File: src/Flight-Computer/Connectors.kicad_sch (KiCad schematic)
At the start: 5 parts

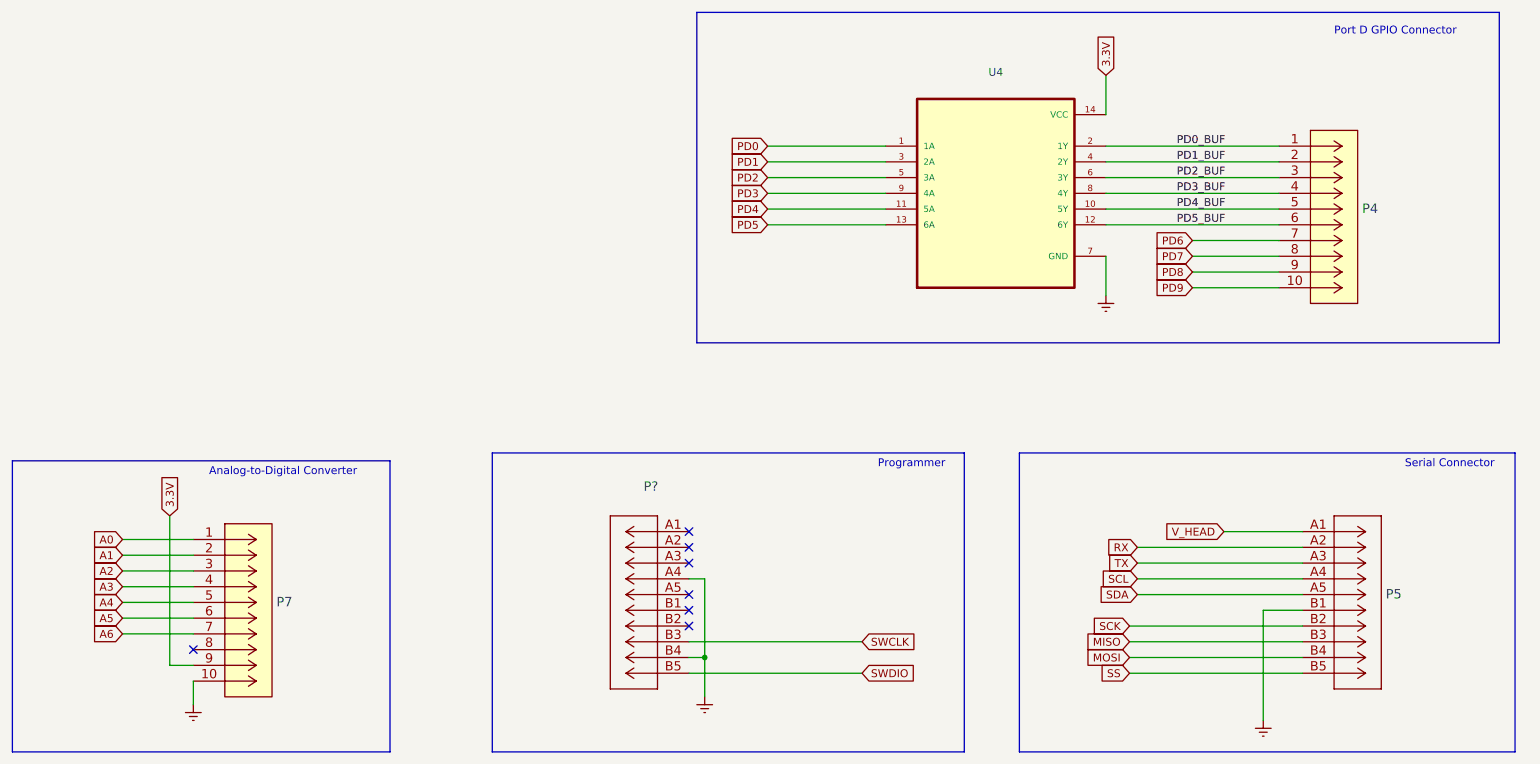
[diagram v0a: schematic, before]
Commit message: implemented crystal oscillator in schematic
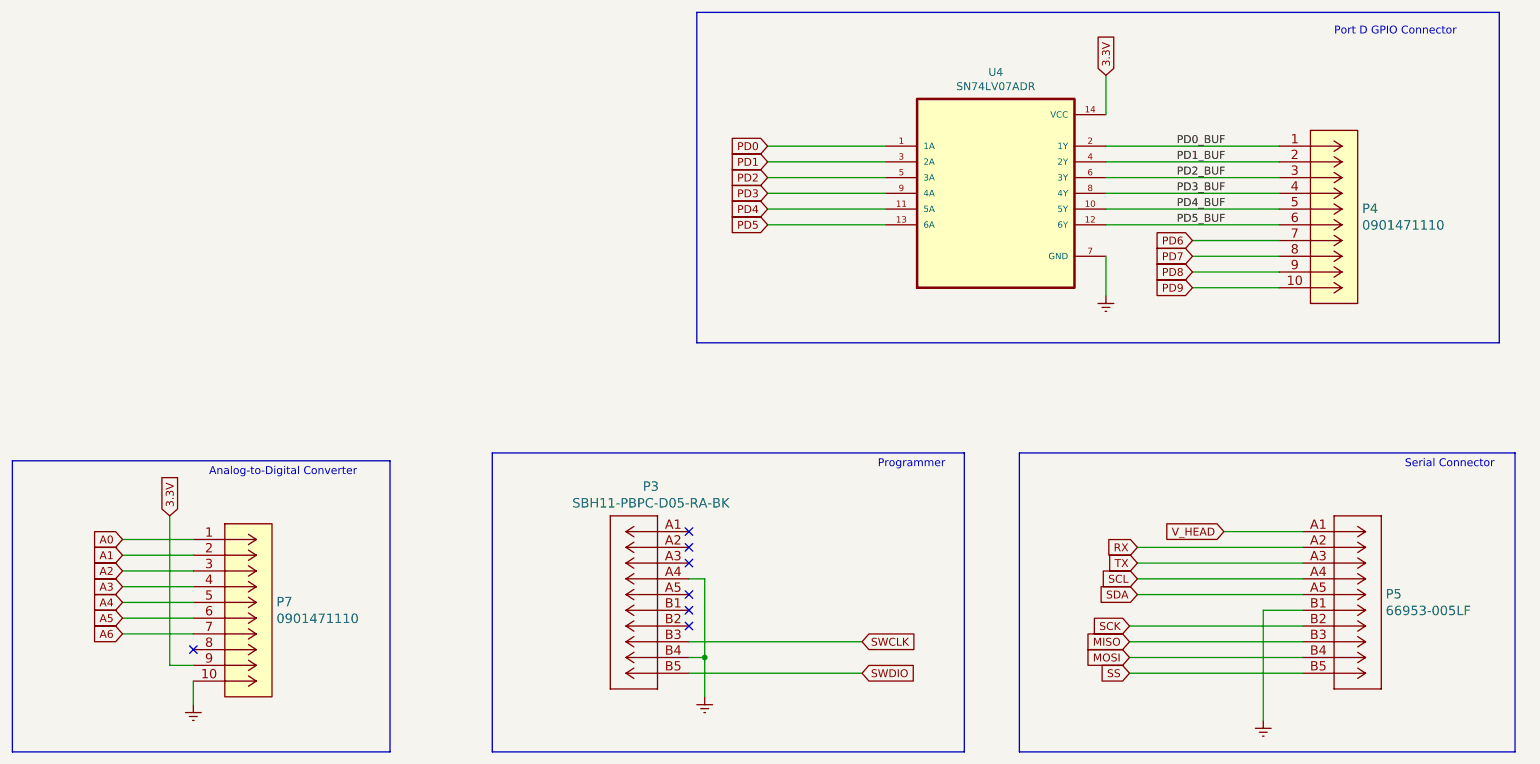
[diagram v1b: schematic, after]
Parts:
- P3: renamed from P?; value (none) -> SBH11-PBPC-D05-RA-BK; footprint (none) -> Engine-Controller:SBH11-PBPC-D05-RA-BK
- P4, P7: value (none) -> 0901471110; footprint (none) -> Engine-Controller:0901471110
- P5: value (none) -> 66953-005LF; footprint (none) -> Engine-Controller:66953-005LF
- U4: value (none) -> SN74LV07ADR; footprint (none) -> Engine-Controller:SN74LV07ADR
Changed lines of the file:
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@@
       (effects (font (size 1.27 1.27)) hide)
     )
-    (property "Value" "" (id 1) (at 223.52 146.05 0)
+    (property "Value" "Earth" (id 1) (at 223.52 146.05 0)
       (effects (font (size 1.27 1.27)) hide)
     )
@@
       (effects (font (size 1.524 1.524)) (justify left))
     )
-    (property "Value" "" (id 1) (at 239.4712 62.3062 0)
+    (property "Value" "0901471110" (id 1) (at 239.4712 62.3062 0)
       (effects (font (size 1.524 1.524)) (justify left))
     )
-    (property "Footprint" "" (id 2) (at 229.87 80.01 0)
+    (property "Footprint" "Engine-Controller:0901471110" (id 2) (at 229.87 80.01 0)
       (effects (font (size 1.524 1.524)) hide)
     )
@@
       (effects (font (size 1.524 1.524)) (justify left))
     )
-    (property "Value" "" (id 1) (at 243.2812 124.5362 0)
+    (property "Value" "66953-005LF" (id 1) (at 243.2812 124.5362 0)
       (effects (font (size 1.524 1.524)) (justify left))
     )
-    (property "Footprint" "" (id 2) (at 233.68 142.24 0)
+    (property "Footprint" "Engine-Controller:66953-005LF" (id 2) (at 233.68 142.24 0)
       (effects (font (size 1.524 1.524)) hide)
     )
@@
     (in_bom yes) (on_board yes)
     (property "Reference" "U4" (id 0) (at 180.34 37.592 0))
-    (property "Value" "" (id 1) (at 180.34 39.9034 0))
-    (property "Footprint" "" (id 2) (at 168.91 80.01 0)
+    (property "Value" "SN74LV07ADR" (id 1) (at 180.34 39.9034 0))
+    (property "Footprint" "Engine-Controller:SN74LV07ADR" (id 2) (at 168.91 80.01 0)
       (effects (font (size 1.27 1.27)) (justify left bottom) hide)
     )
@@
       (effects (font (size 1.27 1.27)) hide)
     )
-    (property "Value" "" (id 1) (at 198.12 77.47 0)
+    (property "Value" "Earth" (id 1) (at 198.12 77.47 0)
       (effects (font (size 1.27 1.27)) hide)
     )
@@
   (symbol (lib_id "Flight-Computer-rescue:Earth-power") (at 133.35 138.43 0) (unit 1)
     (in_bom yes) (on_board yes)
-    (property "Reference" "#PWR?" (id 0) (at 133.35 144.78 0)
+    (property "Reference" "#PWR06" (id 0) (at 133.35 144.78 0)
       (effects (font (size 1.27 1.27)) hide)
     )
-    (property "Value" "" (id 1) (at 133.35 142.24 0)
+    (property "Value" "Earth" (id 1) (at 133.35 142.24 0)
       (effects (font (size 1.27 1.27)) hide)
     )
@@
   (symbol (lib_id "Flight-Computer-rescue:SBH11-PBPC-D05-RA-BK-Engine-Controller") (at 130.81 111.76 0) (mirror y) (unit 1)
     (in_bom yes) (on_board yes)
-    (property "Reference" "P?" (id 0) (at 124.6632 104.4702 0)
+    (property "Reference" "P3" (id 0) (at 124.6632 104.4702 0)
       (effects (font (size 1.524 1.524)))
     )
-    (property "Value" "" (id 1) (at 124.6632 107.1626 0)
+    (property "Value" "SBH11-PBPC-D05-RA-BK" (id 1) (at 124.6632 107.1626 0)
       (effects (font (size 1.524 1.524)))
     )
-    (property "Footprint" "" (id 2) (at 127 142.24 0)
+    (property "Footprint" "Engine-Controller:SBH11-PBPC-D05-RA-BK" (id 2) (at 127 142.24 0)
       (effects (font (size 1.524 1.524)) hide)
     )
@@
       (effects (font (size 1.524 1.524)) (justify left))
     )
-    (property "Value" "" (id 1) (at 64.2112 125.8062 0)
+    (property "Value" "0901471110" (id 1) (at 64.2112 125.8062 0)
       (effects (font (size 1.524 1.524)) (justify left))
     )
-    (property "Footprint" "" (id 2) (at 54.61 143.51 0)
+    (property "Footprint" "Engine-Controller:0901471110" (id 2) (at 54.61 143.51 0)
       (effects (font (size 1.524 1.524)) hide)
     )
@@
       (effects (font (size 1.27 1.27)) hide)
     )
-    (property "Value" "" (id 1) (at 50.8 143.51 0)
+    (property "Value" "Earth" (id 1) (at 50.8 143.51 0)
       (effects (font (size 1.27 1.27)) hide)
     )
